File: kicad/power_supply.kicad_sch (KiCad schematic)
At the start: 22 parts, among them Q701 SIL2300, U701 TP4057, U702 DW01, U703 TPS613222ADBV

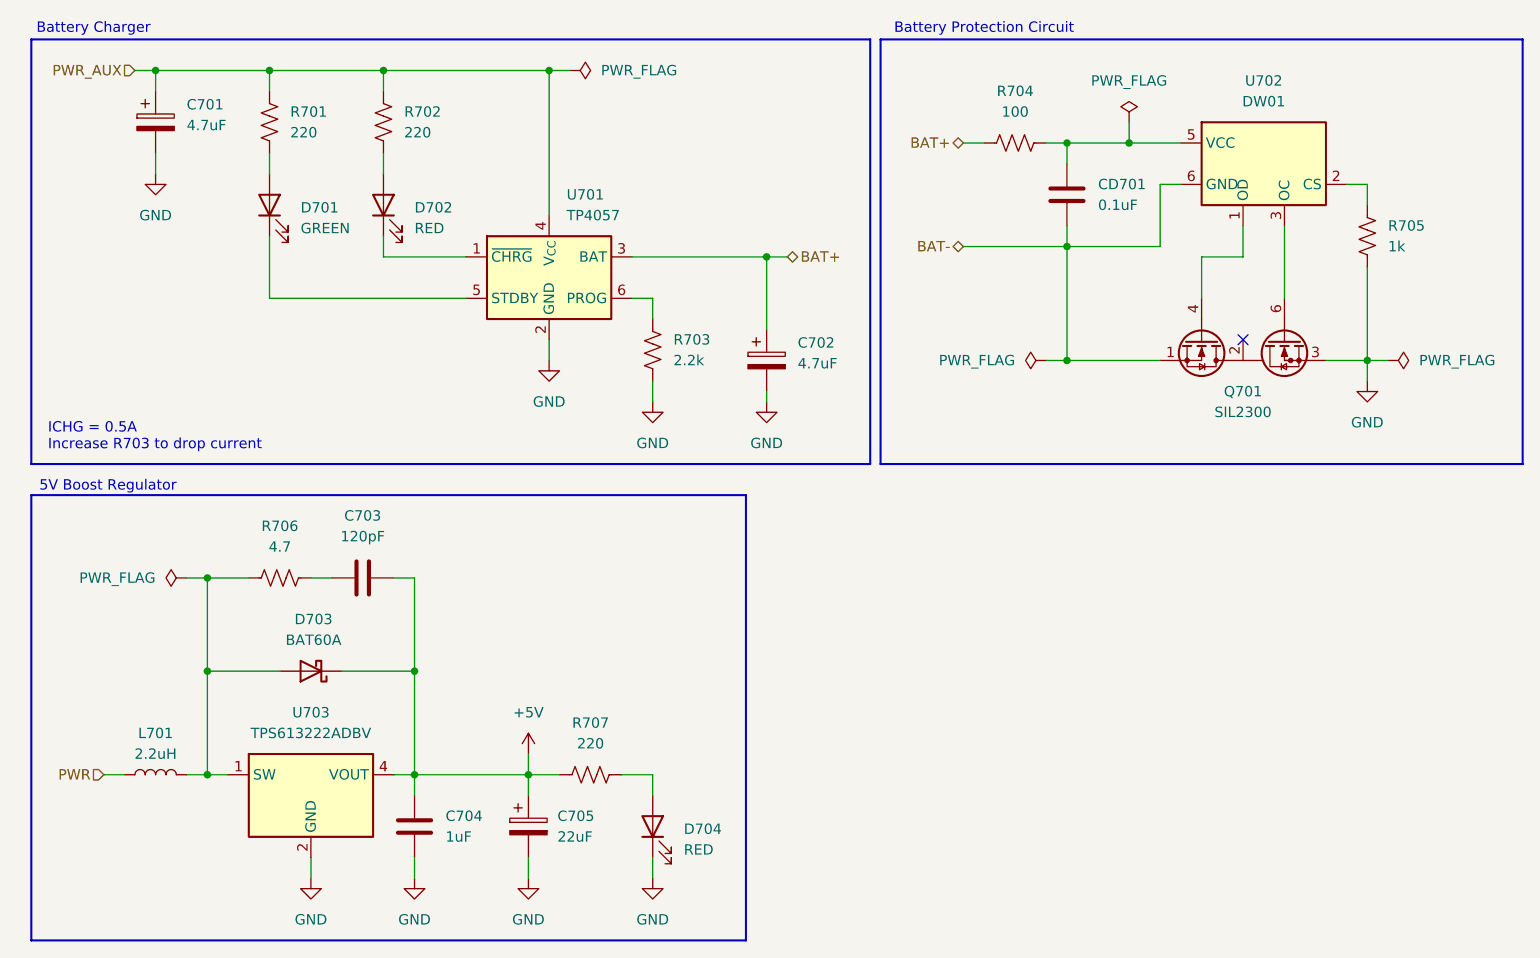
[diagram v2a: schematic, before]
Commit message: ch a voltage reference, ch b hysteresis
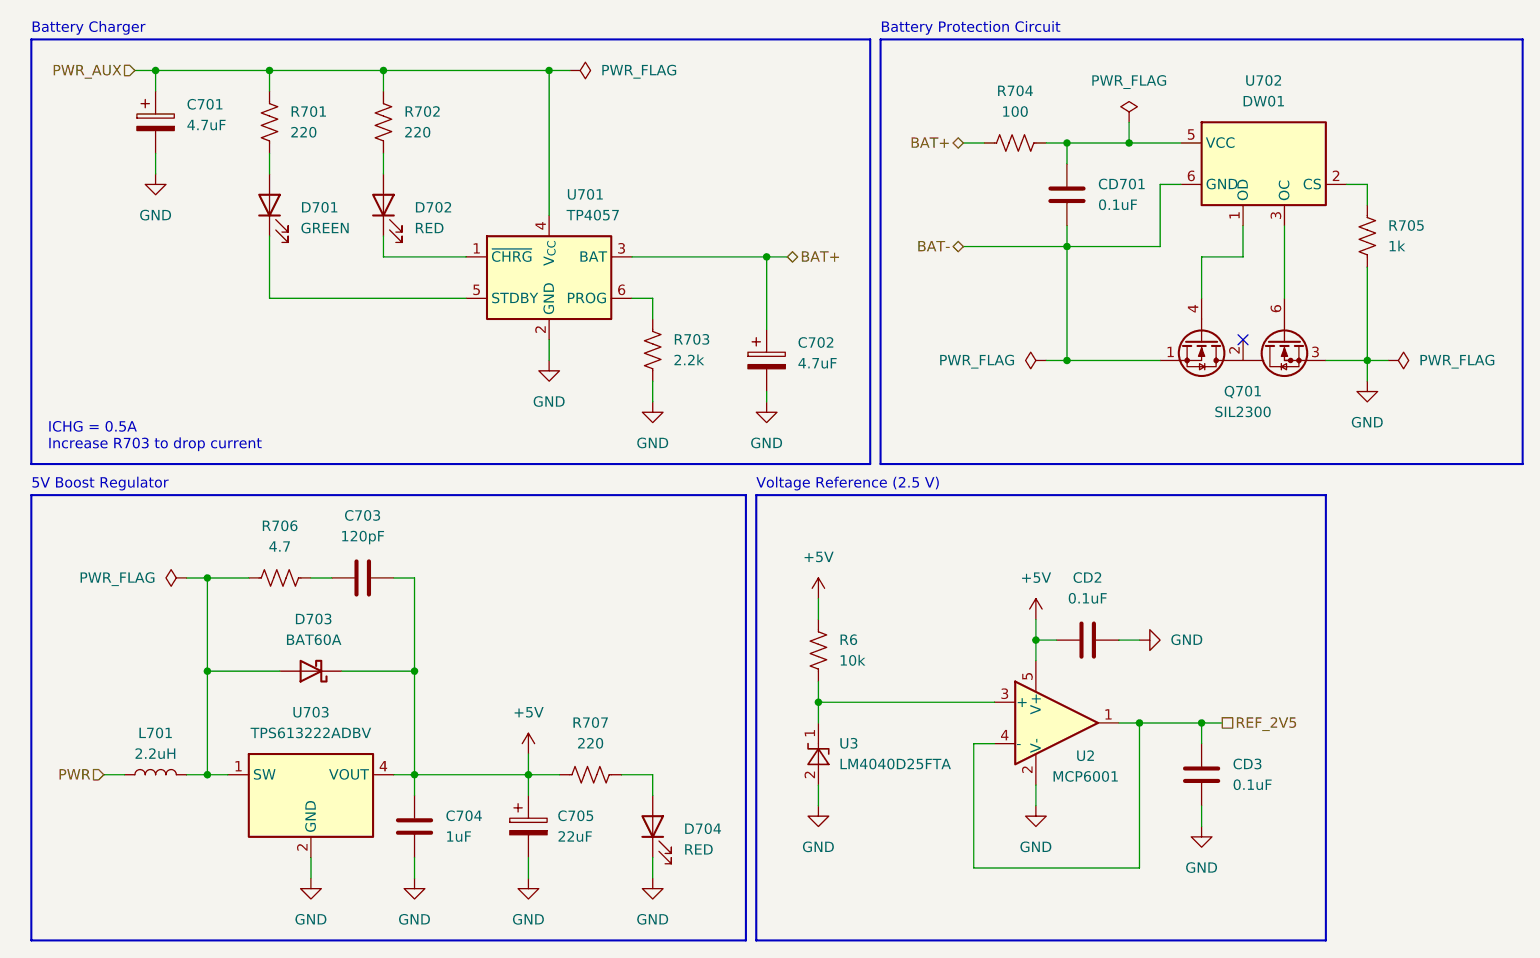
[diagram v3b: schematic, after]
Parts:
- added CD2, CD3: 0.1uF, Custom:C_0402_1005Metric_Fix, symbol Device:C
- added R6: 10k, symbol Device:R_US
- added U2: MCP6001, Package_TO_SOT_SMD:SOT-353_SC-70-5, symbol Amplifier_Operational:MCP6001x-LT
- added U3: LM4040D25FTA, Package_TO_SOT_SMD:SOT-23-3, symbol Reference_Voltage:LM4040DBZ-2.5
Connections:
- net +5V: now also CD2.1, R6.1, U2.5 (V+)
- net GND: now also CD2.2, CD3.2, U2.2 (V-), U3.2 (A)
- new net: R6.2, U2.3 (+), U3.1 (K)
- new net REF_2V5: CD3.1, U2.1, U2.4 (-)
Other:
- note added: "Voltage Reference (2.5 V)"

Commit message: replace alum caps with ceramics, change mpn labeling
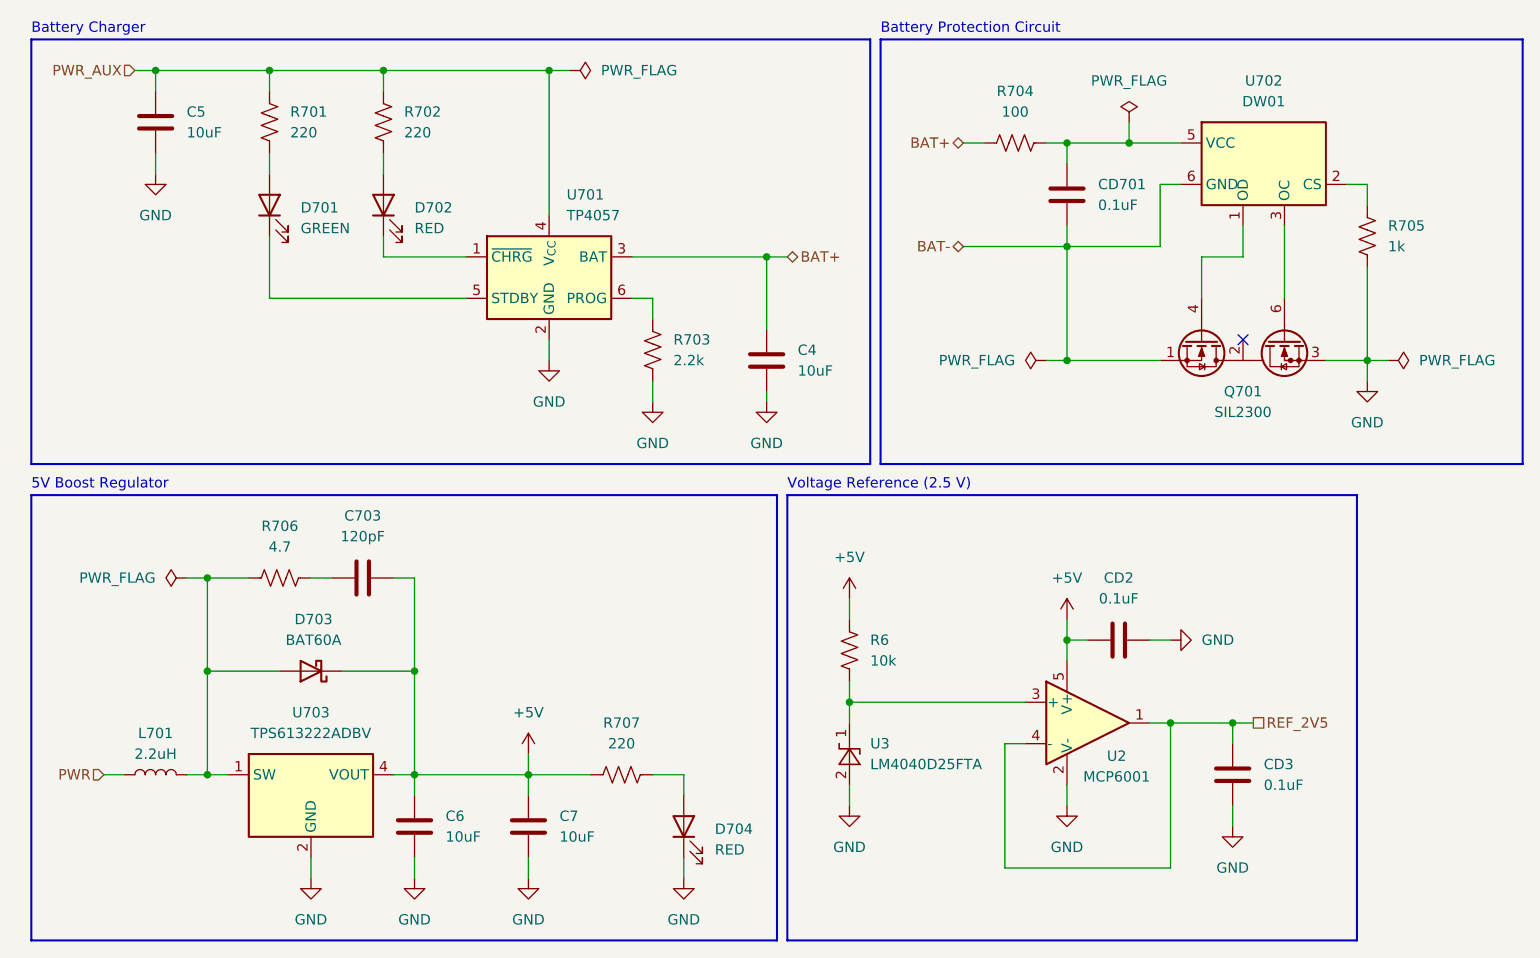
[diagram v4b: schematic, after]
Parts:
- removed C701, C702: 4.7uF, Capacitor_THT:CP_Radial_D5.0mm_P2.00mm, symbol Device:C_Polarized
- removed C704: 1uF, Custom:C_0402_1005Metric_Fix, symbol Device:C
- removed C705: 22uF, Capacitor_THT:CP_Radial_D5.0mm_P2.00mm, symbol Device:C_Polarized
- added C4, C5, C6, C7: 10uF, Capacitor_SMD:C_0603_1608Metric, symbol Device:C
- C703: MPN (none) -> GRM1555C1H121JA01D; Supplier https://www.digikey.com/en/products/detail/murata-electroni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 -> (none)
- CD2, CD3, CD701: MPN (none) -> KGM05AR51C104KH; Supplier https://www.digikey.com/en/products/detail/kyocera-avx/KGM0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 -> (none)
- D701: MPN (none) -> B1911NG--20D000214U1930; Supplier https://www.digikey.com/en/products/detail/harvatek-corpora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 -> (none)
- D702, D704: MPN (none) -> B1911USD-20D000114U1930; Supplier https://www.digikey.com/en/products/detail/harvatek-corpora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 -> (none)
- D703: MPN (none) -> BAT60A; Supplier https://www.digikey.com/en/products/detail/shenzhen-slkormi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 -> (none)
- L701: MPN (none) -> DFE252012F-2R2M=P2; Supplier https://www.digikey.com/en/products/detail/murata-electroni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 -> (none)
- Q701: MPN (none) -> SIL2300-TP; Supplier https://www.digikey.com/en/products/detail/mcc-micro-commer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 -> (none)
- R701, R702, R707: MPN (none) -> RC0402JR-13220RL; Supplier https://www.digikey.com/en/products/detail/yageo/RC0402JR-1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 -> (none)
- R703: MPN (none) -> RC0402JR-132K2L; Supplier https://www.digikey.com/en/products/detail/yageo/RC0402JR-1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 -> (none)
- R704: MPN (none) -> RC0402JR-07100RL; Supplier https://www.digikey.com/en/products/detail/yageo/RC0402JR-0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 -> (none)
- R705: MPN (none) -> RC0402JR-071KL; Supplier https://www.digikey.com/en/products/detail/yageo/RC0402JR-0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 -> (none)
- R706: MPN (none) -> RC0805FR-134R7L; Supplier https://www.digikey.com/en/products/detail/yageo/RC0805FR-1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 -> (none)
- U701: MPN (none) -> TP4057TP4057; Supplier https://www.digikey.com/en/products/detail/evvo/TP4057/2248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 -> (none)
- U702: MPN (none) -> DW01; Supplier https://www.digikey.com/en/products/detail/evvo/DW01/262210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 -> (none)
- U703: MPN (none) -> TPS613222ADBVR; Supplier https://www.digikey.com/en/products/detail/texas-instrument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 -> (none)
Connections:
- net +5V: now also C6.1, C7.1
- net BAT+: now also C4.1
- net GND: now also C4.2, C5.2, C6.2, C7.2
- net PWR_AUX: now also C5.1
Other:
- note removed: "ICHG = 0.5A Increase R703 to drop current"
- moved on the sheet: CD2, CD3, D704, R6, R707, U2, U3

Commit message: finish 2.0 part selection
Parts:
- R6: footprint (none) -> Custom:R_0402_1005Metric_Fix; MPN (none) -> RC0402JR-1310KL
- U2: MPN (none) -> MCP6001T-I/OT
- U3: MPN (none) -> LM4040D25FTA
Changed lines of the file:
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@@
 	(title_block
 		(title "Frequency Counter")
-		(date "2026-02-17")
+		(date "2026-02-18")
 		(rev "2.0-draft")
 		(company "vladaviedov.org")
@@
 			)
 		)
-		(property "Supplier" ""
-			(at 49.53 86.36 90)
-			(effects
-				(font
-					(size 1.27 1.27)
-				)
-				(hide yes)
-			)
-		)
 		(property "MPN" "RC0805FR-134R7L"
 			(at 49.53 86.36 90)
@@
 			)
 		)
-		(property "Supplier" ""
-			(at 34.29 110.49 90)
-			(effects
-				(font
-					(size 1.27 1.27)
-				)
-				(hide yes)
-			)
-		)
 		(property "MPN" "DFE252012F-2R2M=P2"
 			(at 34.29 110.49 90)
@@
 			)
 		)
-		(property "Supplier" ""
-			(at 99.06 116.84 0)
-			(effects
-				(font
-					(size 1.27 1.27)
-				)
-				(hide yes)
-			)
-		)
 		(property "MPN" "B1911USD-20D000114U1930"
 			(at 99.06 116.84 90)
@@
 			)
 		)
-		(property "Supplier" ""
-			(at 91.44 110.49 90)
-			(effects
-				(font
-					(size 1.27 1.27)
-				)
-				(hide yes)
-			)
-		)
 		(property "MPN" "RC0402JR-13220RL"
 			(at 91.44 110.49 90)
@@
 			)
 		)
-		(property "Supplier" ""
-			(at 62.23 30.48 0)
-			(effects
-				(font
-					(size 1.27 1.27)
-				)
-				(hide yes)
-			)
-		)
 		(property "MPN" "RC0402JR-13220RL"
 			(at 62.23 30.48 0)
@@
 			)
 		)
-		(property "Supplier" ""
-			(at 59.69 86.36 90)
-			(effects
-				(font
-					(size 1.27 1.27)
-				)
-				(hide yes)
-			)
-		)
 		(property "MPN" "GRM1555C1H121JA01D"
 			(at 59.69 86.36 90)
@@
 			)
 		)
-		(property "Supplier" ""
-			(at 139.7 33.02 90)
-			(effects
-				(font
-					(size 1.27 1.27)
-				)
-				(hide yes)
-			)
-		)
 		(property "MPN" "RC0402JR-07100RL"
 			(at 139.7 33.02 90)
@@
 			)
 		)
-		(property "Supplier" ""
-			(at 146.05 39.37 0)
-			(effects
-				(font
-					(size 1.27 1.27)
-				)
-				(hide yes)
-			)
-		)
 		(property "MPN" "KGM05AR51C104KH"
 			(at 146.05 39.37 0)
@@
 			)
 		)
-		(property "Supplier" ""
-			(at 167.64 59.69 90)
-			(effects
-				(font
-					(size 1.27 1.27)
-				)
-				(hide yes)
-			)
-		)
 		(property "MPN" "SIL2300-TP "
 			(at 167.64 59.69 90)
@@
 			)
 		)
-		(property "Supplier" ""
-			(at 82.55 49.53 0)
-			(effects
-				(font
-					(size 1.27 1.27)
-				)
-				(hide yes)
-			)
-		)
 		(property "MPN" "TP4057TP4057"
 			(at 82.55 49.53 0)
@@
 			)
 		)
-		(property "Supplier" ""
-			(at 48.26 40.64 90)
-			(effects
-				(font
-					(size 1.27 1.27)
-				)
-				(hide yes)
-			)
-		)
 		(property "MPN" "B1911NG--20D000214U1930"
 			(at 48.26 40.64 90)
@@
 			)
 		)
+		(property "MPN" "LM4040D25FTA"
+			(at 119.38 107.95 90)
+			(effects
+				(font
+					(size 1.27 1.27)
+				)
+				(hide yes)
+			)
+		)
 		(pin "1"
 		)
@@
 			)
 		)
-		(property "Supplier" ""
-			(at 166.37 110.49 0)
-			(effects
-				(font
-					(size 1.27 1.27)
-				)
-				(hide yes)
-			)
-		)
 		(property "MPN" "KGM05AR51C104KH"
 			(at 166.37 110.49 0)
@@
 			)
 		)
-		(property "Supplier" ""
-			(at 170.18 35.56 0)
-			(effects
-				(font
-					(size 1.27 1.27)
-				)
-				(hide yes)
-			)
-		)
 		(property "MPN" "DW01"
 			(at 170.18 35.56 0)
@@
 			)
 		)
-		(property "Supplier" ""
-			(at 182.88 44.45 0)
-			(effects
-				(font
-					(size 1.27 1.27)
-				)
-				(hide yes)
-			)
-		)
 		(property "MPN" "RC0402JR-071KL "
 			(at 182.88 44.45 0)
@@
 			)
 		)
-		(property "Supplier" ""
-			(at 62.23 40.64 90)
-			(effects
-				(font
-					(size 1.27 1.27)
-				)
-				(hide yes)
-			)
-		)
 		(property "MPN" "B1911USD-20D000114U1930"
 			(at 62.23 40.64 90)
@@
 			)
 		)
+		(property "MPN" "MCP6001T-I/OT "
+			(at 148.59 104.14 0)
+			(effects
+				(font
+					(size 1.27 1.27)
+				)
+				(hide yes)
+			)
+		)
 		(pin "3"
 		)
@@
 			)
 		)
-		(property "Supplier" ""
-			(at 53.34 97.79 0)
-			(effects
-				(font
-					(size 1.27 1.27)
-				)
-				(hide yes)
-			)
-		)
 		(property "MPN" "BAT60A"
 			(at 53.34 97.79 0)
@@
 			)
 		)
-		(property "Supplier" ""
-			(at 53.34 113.03 0)
-			(effects
-				(font
-					(size 1.27 1.27)
-				)
-				(hide yes)
-			)
-		)
 		(property "MPN" "TPS613222ADBVR"
 			(at 53.34 113.03 0)
@@
 			)
 		)
-		(property "Footprint" ""
+		(property "Footprint" "Custom:R_0402_1005Metric_Fix"
 			(at 120.396 95.504 90)
 			(effects
@@
 			)
 		)
+		(property "MPN" "RC0402JR-1310KL"
+			(at 119.38 95.25 0)
+			(effects
+				(font
+					(size 1.27 1.27)
+				)
+				(hide yes)
+			)
+		)
 		(pin "1"
 		)
@@
 			)
 		)
-		(property "Supplier" ""
-			(at 48.26 30.48 0)
-			(effects
-				(font
-					(size 1.27 1.27)
-				)
-				(hide yes)
-			)
-		)
 		(property "MPN" "RC0402JR-13220RL"
 			(at 48.26 30.48 0)
@@
 			)
 		)
-		(property "Supplier" ""
-			(at 152.4 93.98 0)
-			(effects
-				(font
-					(size 1.27 1.27)
-				)
-				(hide yes)
-			)
-		)
 		(property "MPN" "KGM05AR51C104KH"
 			(at 152.4 93.98 90)
@@
 			(at 95.25 58.42 0)
 			(effects
-				(font
-					(size 1.27 1.27)
-				)
-				(hide yes)
-			)
-		)
-		(property "Supplier" ""
-			(at 95.25 58.42 0)
-			(effects

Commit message: assign references
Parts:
- renumbered C5 to C801, C4 to C802, C703 to C803, C6 to C804, C7 to C805, CD701 to CD801, CD2 to CD802, CD3 to CD803, D701 to D801, D702 to D802, D703 to D803, D704 to D804, L701 to L801, Q701 to Q801, R701 to R801, R702 to R802, R703 to R803, R704 to R804, R705 to R805, R6 to R806, R706 to R807, R707 to R808, U701 to U801, U702 to U802, U3 to U803, U2 to U804, U703 to U805
